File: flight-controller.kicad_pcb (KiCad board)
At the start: 2 copper layers, 0 parts

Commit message: chore: Initialized pcb
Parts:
- added BZ1: Buzzer, Buzzer_Beeper:Buzzer_12x9.5RM7.6, F.Cu at (52.6, 25.6)
- added C1: 100nF, Capacitor_SMD:C_0402_1005Metric, F.Cu at (39.6, 47.3)
- added C2: 100nF, Capacitor_SMD:C_0402_1005Metric, F.Cu at (39.6, 49.3)
- added C3: 100nF, Capacitor_SMD:C_0402_1005Metric, F.Cu at (39.6, 51.3)
- added C4: 100nF, Capacitor_SMD:C_0402_1005Metric, F.Cu at (39.6, 53.2)
- added C5: 100uF, Capacitor_THT:CP_Radial_D6.3mm_P2.50mm, F.Cu at (54.6, 45.2)
- added C6: 100nF, Capacitor_SMD:C_0402_1005Metric, F.Cu at (39.6, 55.2)
- added CN10: Conn_02x17_Odd_Even, Connector_PinHeader_2.54mm:PinHeader_2x17_P2.54mm_Vertical, F.Cu at (23.2, 21.2)
- added CN7: Conn_02x10_Odd_Even, Connector_PinHeader_2.54mm:PinHeader_2x10_P2.54mm_Vertical, F.Cu at (37.6, 21.2)
- added CN8: Conn_02x08_Odd_Even, Connector_PinHeader_2.54mm:PinHeader_2x08_P2.54mm_Vertical, F.Cu at (44.8, 21.2)
- added CN9: Conn_02x15_Odd_Even, Connector_PinHeader_2.54mm:PinHeader_2x15_P2.54mm_Vertical, F.Cu at (30.4, 21.2)
- added D1: LED_RGBK, LED_THT:LED_D5.0mm-4_RGB, F.Cu at (53.6, 52.9)
- added D2: 1N4148, Diode_THT:D_DO-35_SOD27_P7.62mm_Horizontal, F.Cu at (53.3, 58.4)
- added D3: SS14, Diode_SMD:D_SOD-123, F.Cu at (52.6, 34.1)
- added D4: SS14, Diode_SMD:D_SOD-123, F.Cu at (52.6, 37.4)
- added J1: Conn_01x04, Connector_PinHeader_2.54mm:PinHeader_1x04_P2.54mm_Vertical, F.Cu at (49.4, 43.6)
- added J7: J_ESC_POWER, Connector_PinHeader_2.54mm:PinHeader_1x02_P2.54mm_Vertical, F.Cu at (49.4, 55.8)
- added JBN880: Conn_01x06, Connector_PinHeader_2.54mm:PinHeader_1x06_P2.54mm_Vertical, F.Cu at (44.8, 43.6)
- added Q1: 2N2222, Package_TO_SOT_THT:TO-92_Inline, F.Cu at (57.4, 35.6)
- added R1: 4.7kΩ, Resistor_SMD:R_0402_1005Metric, F.Cu at (36.7, 47.3)
- added R2: 4.7kΩ, Resistor_SMD:R_0402_1005Metric, F.Cu at (36.7, 49.3)
- added R3: 150Ω, Resistor_SMD:R_0402_1005Metric, F.Cu at (36.7, 51.3)
- added R4: 33Ω, Resistor_SMD:R_0402_1005Metric, F.Cu at (36.7, 53.3)
- added R5: 33Ω, Resistor_SMD:R_0402_1005Metric, F.Cu at (36.7, 55.3)
- added R6: 1kΩ, Resistor_SMD:R_0402_1005Metric, F.Cu at (36.7, 57.3)
- added U1: BMI088, fc_library:BMI088, F.Cu at (38.3, 61.1)
- added U2: BMP390, fc_library:BMP390L, F.Cu at (44.2, 60.9)

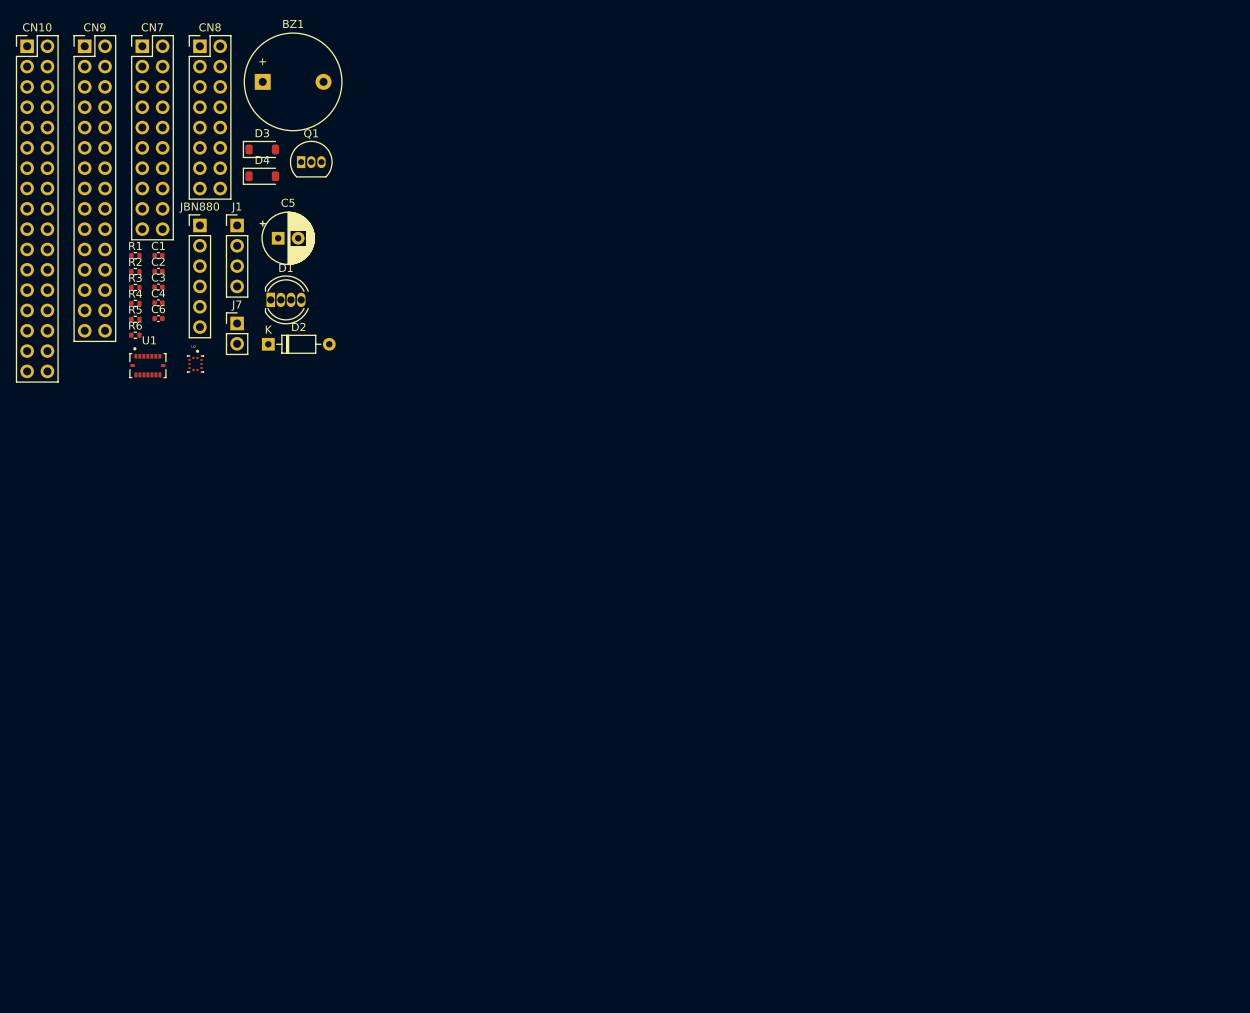
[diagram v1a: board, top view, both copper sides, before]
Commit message: feat: Placed CN connectors on right location
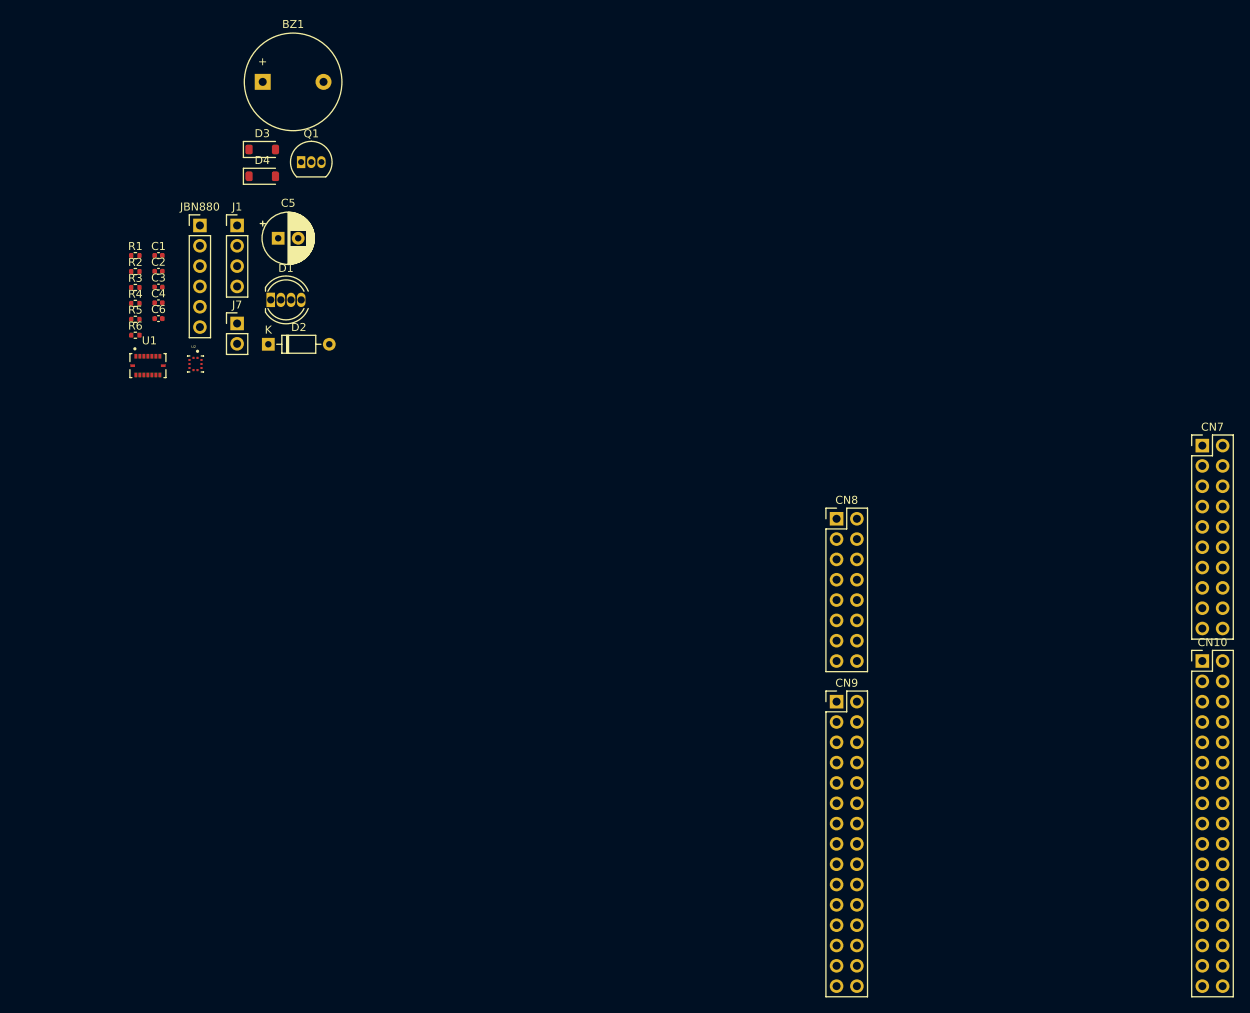
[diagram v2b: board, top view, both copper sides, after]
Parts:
- moved CN10 165.8 mm to (170.1, 98.0)
- moved CN7 141.6 mm to (170.1, 71.1)
- moved CN9 124.7 mm to (124.4, 103.1)
- moved CN8 99.1 mm to (124.4, 80.2)
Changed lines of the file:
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@@
   )
   (setup
+    (stackup
+      (layer "F.SilkS" (type "Top Silk Screen"))
+      (layer "F.Paste" (type "Top Solder Paste"))
+      (layer "F.Mask" (type "Top Solder Mask") (thickness 0.01))
+      (layer "F.Cu" (type "copper") (thickness 0.035))
+      (layer "dielectric 1" (type "core") (thickness 1.51) (material "FR4") (epsilon_r 4.5) (loss_tangent 0.02))
+      (layer "B.Cu" (type "copper") (thickness 0.035))
+      (layer "B.Mask" (type "Bottom Solder Mask") (thickness 0.01))
+      (layer "B.Paste" (type "Bottom Solder Paste"))
+      (layer "B.SilkS" (type "Bottom Silk Screen"))
+      (copper_finish "None")
+      (dielectric_constraints no)
+    )
     (pad_to_mask_clearance 0)
     (pcbplotparams
@@
   )
   (footprint "Connector_PinHeader_2.54mm:PinHeader_2x17_P2.54mm_Vertical" (layer "F.Cu")
-    (at 23.19 21.17)
+    (at 170.0911 98.013035)
     (descr "Through hole straight pin header, 2x17, 2.54mm pitch, double rows")
     (tags "Through hole pin header THT 2x17 2.54mm double row")
@@
   )
   (footprint "Connector_PinHeader_2.54mm:PinHeader_2x15_P2.54mm_Vertical" (layer "F.Cu")
-    (at 30.39 21.17)
+    (at 124.3711 103.093035)
     (descr "Through hole straight pin header, 2x15, 2.54mm pitch, double rows")
     (tags "Through hole pin header THT 2x15 2.54mm double row")
@@
   )
   (footprint "Connector_PinHeader_2.54mm:PinHeader_2x08_P2.54mm_Vertical" (layer "F.Cu")
-    (at 44.79 21.17)
+    (at 124.3711 80.233035)
     (descr "Through hole straight pin header, 2x08, 2.54mm pitch, double rows")
     (tags "Through hole pin header THT 2x08 2.54mm double row")
@@
   )
   (footprint "Connector_PinHeader_2.54mm:PinHeader_2x10_P2.54mm_Vertical" (layer "F.Cu")
-    (at 37.59 21.17)
+    (at 170.0911 71.089035)
     (descr "Through hole straight pin header, 2x10, 2.54mm pitch, double rows")
     (tags "Through hole pin header THT 2x10 2.54mm double row")
